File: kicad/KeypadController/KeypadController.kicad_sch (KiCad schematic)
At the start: 16 parts, among them J1 ISP, J2 Keypad, J3 Switch, J4 Keypad, U1 MAX232, U2 ATmega48-20P

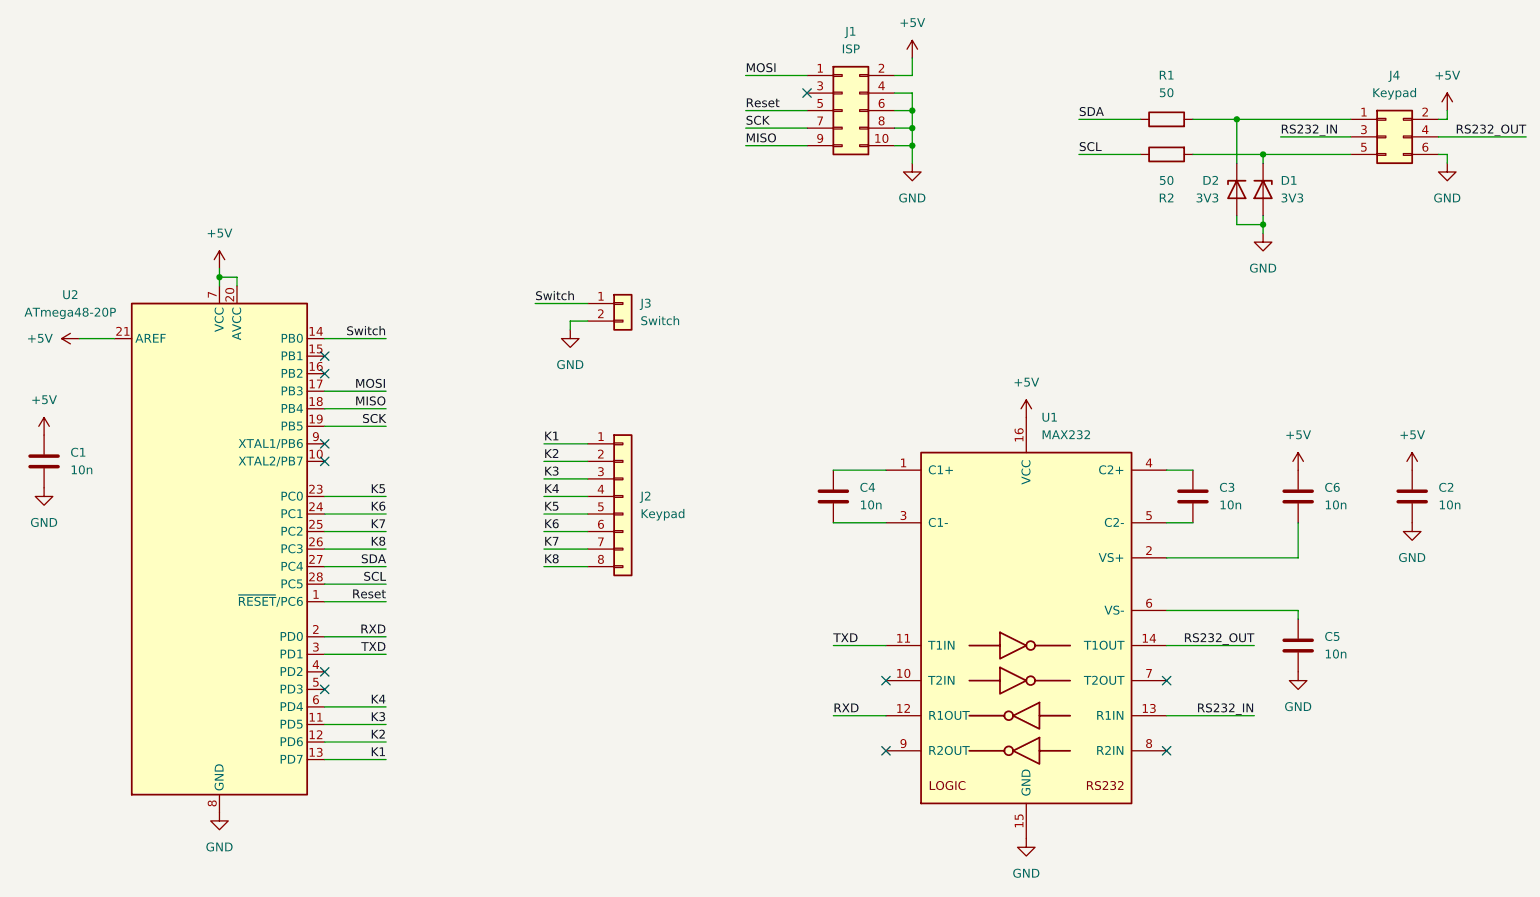
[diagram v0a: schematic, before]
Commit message: Added interrupt for Raspberry PI I2C
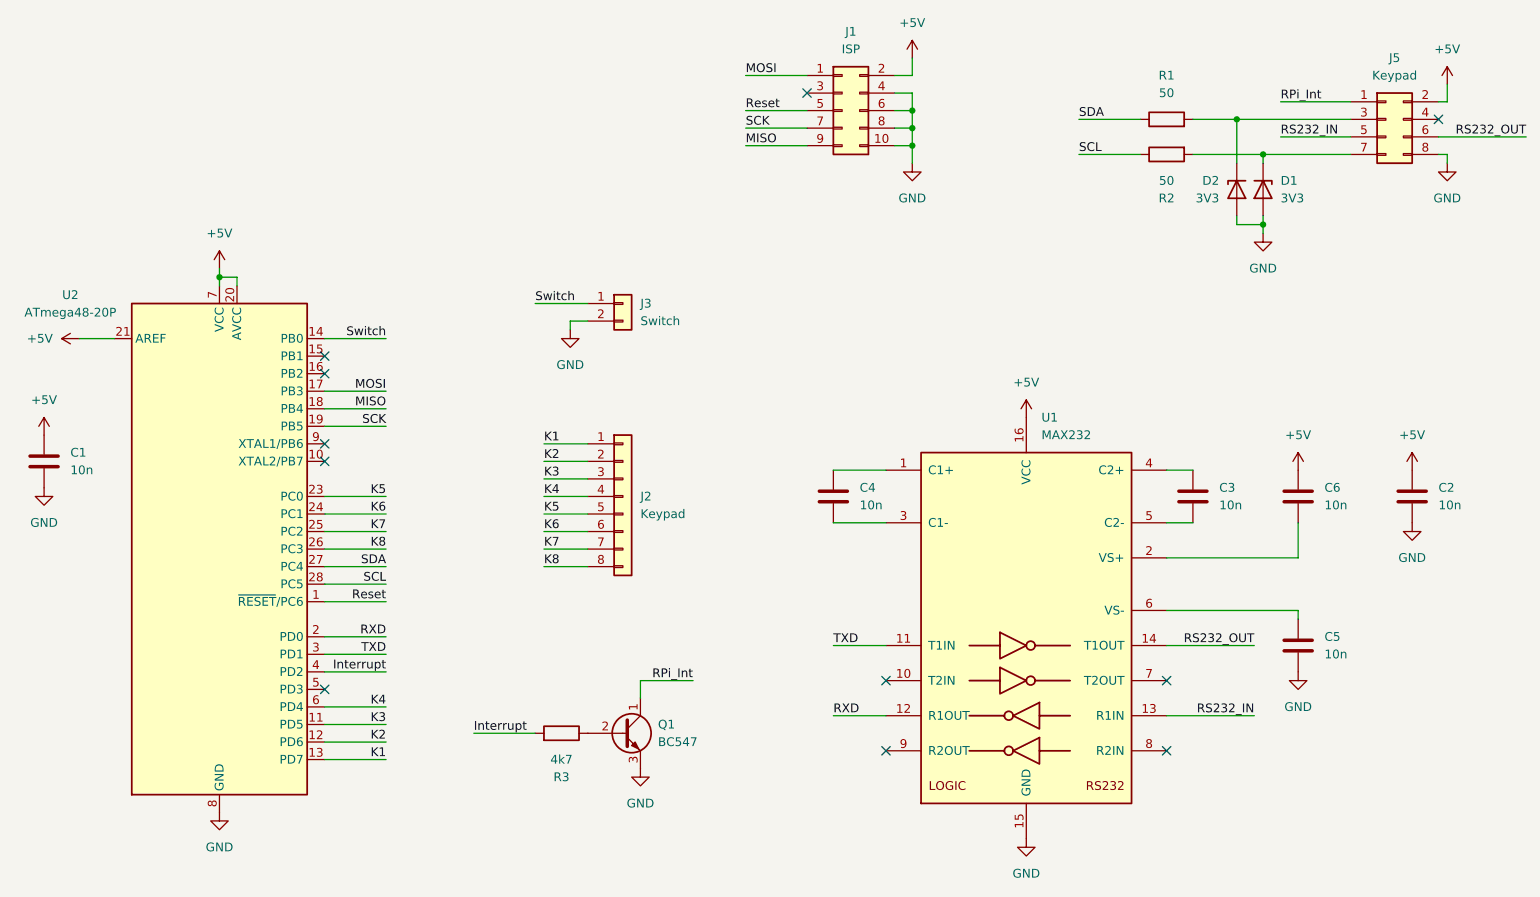
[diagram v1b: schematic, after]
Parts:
- removed J4: Keypad, symbol Connector_Generic:Conn_02x03_Odd_Even
- added J5: Keypad, symbol Connector_Generic:Conn_02x04_Odd_Even
- added Q1: BC547, Package_TO_SOT_THT:TO-92L_Inline, symbol Transistor_BJT:BC547
- added R3: 4k7, Resistor_THT:R_Axial_DIN0207_L6.3mm_D2.5mm_P2.54mm_Vertical, symbol Device:R
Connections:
- net +5V: now also J5.2 (Pin_2)
- net GND: now also J5.8 (Pin_8), Q1.3 (E)
- net RS232_IN: now also J5.5 (Pin_5)
- net RS232_OUT: now also J5.6 (Pin_6)
- net Interrupt: now reaches U2.4 (PD2)
- net Interrupt: now also R3.2
- net at D1.1 (K), R2.2: now also J5.7 (Pin_7)
- net at D2.1 (K), R1.2: now also J5.3 (Pin_3)
- new net: Q1.2 (B), R3.1
- new net RPi_Int: J5.1 (Pin_1), Q1.1 (C)
